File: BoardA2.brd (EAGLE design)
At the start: 44 x 93 mm, 18 parts, among them J1 FEMALE 2x3, T1 2N2222

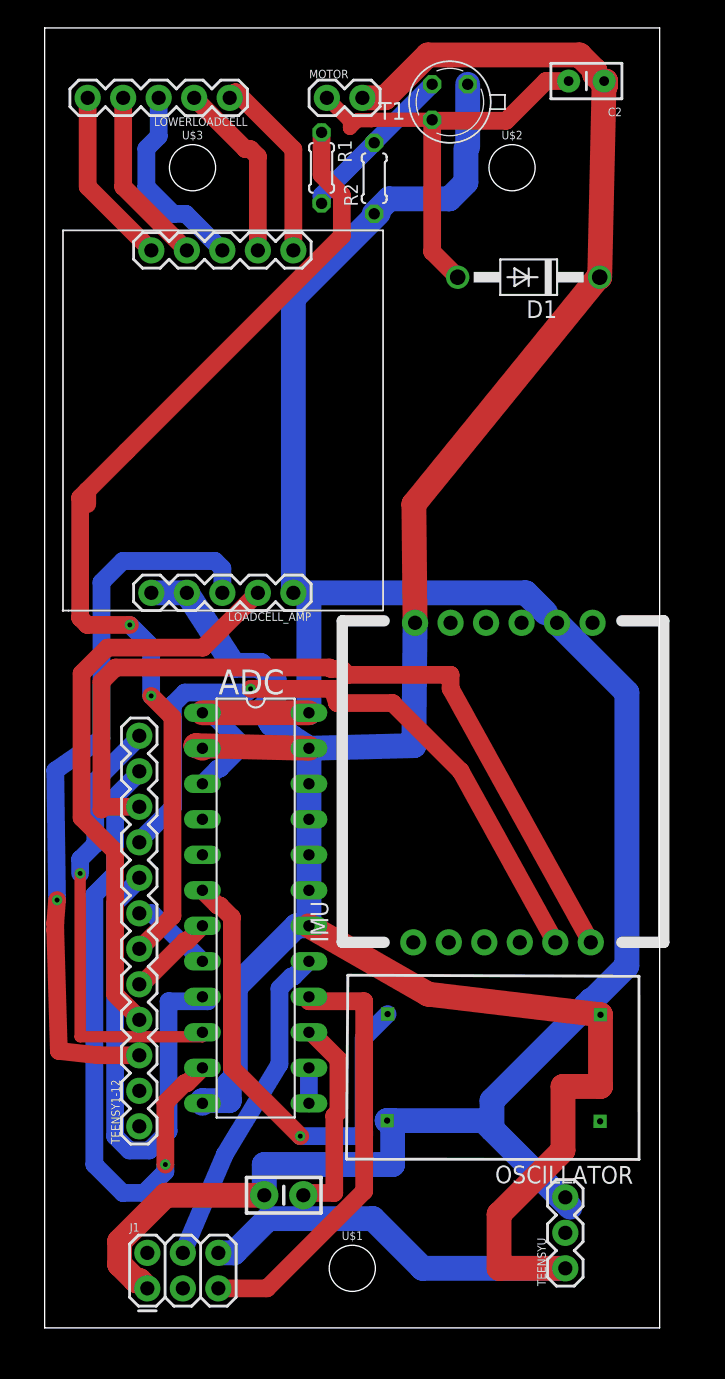
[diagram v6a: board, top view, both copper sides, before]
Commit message: Board2 Missing signal
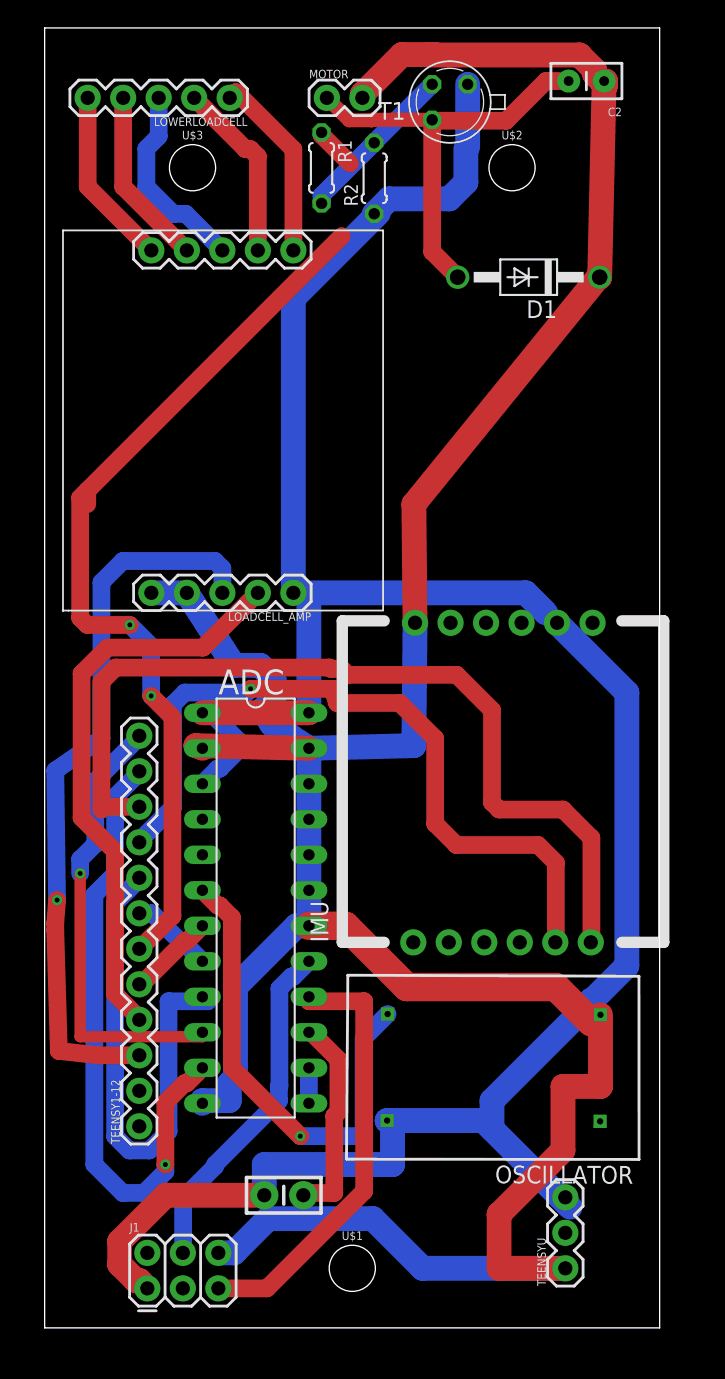
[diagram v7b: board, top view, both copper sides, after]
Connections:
- removed net ADC-CONVST: ADC.5
- new net ADC-CON: ADC.5, TEENSY1-12.2
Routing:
- net MOTOR: track 73.3 -> 68.3 mm
- net IMU-TX: track 48.7 -> 53.5 mm
- net IMU-RX: track 59.3 -> 63.8 mm
- net 5V: track 214.8 -> 216.3 mm
- net ADC-CH2: track 23.5 -> 24.7 mm
- net N$6: track 31.9 -> 31.2 mm
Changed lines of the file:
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@@
 <setting verticaltext="up"/>
 </settings>
-<grid distance="20" unitdist="mil" unit="mm" style="dots" multiple="1" display="yes" altdistance="5" altunitdist="mil" altunit="mm"/>
+<grid distance="20" unitdist="mil" unit="mil" style="dots" multiple="1" display="yes" altdistance="5" altunitdist="mil" altunit="mil"/>
 <layers>
 <layer number="1" name="Top" color="4" fill="1" visible="yes" active="yes"/>
@@
 <wire x1="-2.564" y1="91.5" x2="-2.564" y2="0.96" width="0.1524" layer="231"/>
 <dimension x1="0" y1="0" x2="7.3152" y2="3.429" x3="3.6576" y3="-3.048" textsize="1.778" layer="1" dtype="horizontal"/>
+<dimension x1="6.77" y1="14.42" x2="37.25" y2="4.26" x3="22.01" y3="-7.112" textsize="1.778" layer="1" dtype="horizontal"/>
 </plain>
 <attributes>
@@
 <wire x1="18.907" y1="36.385" x2="18.907" y2="38.925" width="1.778" layer="16"/>
 <wire x1="18.907" y1="38.925" x2="18.907" y2="41.465" width="1.778" layer="16"/>
-<wire x1="18.907" y1="28.765" x2="27.432" y2="23.876" width="1.778" layer="1"/>
-<wire x1="27.432" y1="23.876" x2="39.76725" y2="22.397375" width="1.778" layer="1"/>
 <wire x1="18.907" y1="41.465" x2="10.8204" y2="41.652465625" width="1.778" layer="1"/>
 <wire x1="10.8204" y1="41.652465625" x2="11.287" y2="41.465" width="1.778" layer="1"/>
@@
 <wire x1="18.0242875" y1="28.765" x2="18.907" y2="28.765" width="1.778" layer="16"/>
 <wire x1="13.6492" y1="17.9000875" x2="13.6492" y2="24.3899125" width="1.778" layer="16"/>
-<wire x1="22.731" y1="88" x2="24.3472875" y2="88" width="1.778" layer="1"/>
-<wire x1="24.3472875" y1="88" x2="27.4161875" y2="91.0689" width="1.778" layer="1"/>
+<wire x1="18.907" y1="28.765" x2="21.527" y2="28.765" width="2.032" layer="1"/>
+<wire x1="21.527" y1="28.765" x2="25.908" y2="24.384" width="2.032" layer="1"/>
+<wire x1="36.576" y1="24.384" x2="39.116" y2="21.844" width="2.032" layer="1"/>
+<wire x1="25.908" y1="24.384" x2="36.576" y2="24.384" width="2.032" layer="1"/>
+<wire x1="22.731" y1="88" x2="22.731" y2="88.263" width="1.778" layer="1"/>
+<wire x1="22.731" y1="88.263" x2="25.563" y2="91.095" width="1.778" layer="1"/>
+<wire x1="25.563" y1="91.095" x2="27.94" y2="91.095" width="1.778" layer="1"/>
+<wire x1="27.4161875" y1="91.0689" x2="27.94" y2="91.095" width="0" layer="19" extent="1-1"/>
+<wire x1="39.76725" y1="22.397375" x2="39.116" y2="21.844" width="0" layer="19" extent="1-1"/>
 </signal>
 <signal name="N$1">
@@
 <wire x1="27.724" y1="86.43" x2="23.424025" y2="86.43" width="1.016" layer="1"/>
 <wire x1="23.424025" y1="86.43" x2="23.393825" y2="86.3998" width="1.016" layer="1"/>
-<wire x1="23.393825" y1="86.3998" x2="22.3918" y2="86.3998" width="1.016" layer="1"/>
-<wire x1="22.3918" y1="86.3998" x2="21.844" y2="85.852" width="1.016" layer="1"/>
-<wire x1="21.844" y1="85.852" x2="21.844" y2="86.347" width="1.016" layer="1"/>
-<wire x1="21.844" y1="86.347" x2="20.191" y2="88" width="1.016" layer="1"/>
+<wire x1="23.424025" y1="86.43" x2="23.393825" y2="86.3998" width="1.016" layer="1"/>
+<wire x1="23.393825" y1="86.3998" x2="21.7912" y2="86.3998" width="1.016" layer="1"/>
+<wire x1="21.7912" y1="86.3998" x2="20.191" y2="88" width="1.016" layer="1"/>
 </signal>
 <signal name="N$8">
@@
 <wire x1="6.096" y1="50.292" x2="3.048" y2="50.292" width="1.27" layer="1"/>
 <wire x1="3.048" y1="50.292" x2="2.54" y2="50.8" width="1.27" layer="1"/>
-<wire x1="3.048" y1="58.928" x2="3.048" y2="59.89836875" width="1.27" layer="1"/>
-<wire x1="21.2598" y1="81.0467" x2="19.812" y2="82.4945" width="1.27" layer="1"/>
-<wire x1="19.812" y1="82.4945" x2="19.812" y2="85.527" width="1.27" layer="1"/>
-<wire x1="3.048" y1="59.89836875" x2="5.864815625" y2="62.715184375" width="1.27" layer="1"/>
-<wire x1="5.864815625" y1="62.715184375" x2="21.2598" y2="78.11016875" width="1.27" layer="1"/>
-<wire x1="21.2598" y1="78.11016875" x2="21.2598" y2="81.0467" width="1.27" layer="1"/>
+<wire x1="3.048" y1="59.89836875" x2="3.048" y2="58.928" width="1.27" layer="1"/>
+<wire x1="21.2598" y1="81.0467" x2="19.812" y2="82.4945" width="0" layer="19" extent="1-16"/>
+<wire x1="21.844" y1="83.312" x2="21.2598" y2="78.11016875" width="0" layer="19" extent="1-16"/>
+<wire x1="21.2598" y1="78.11016875" x2="3.048" y2="59.89836875" width="1.27" layer="1"/>
+<wire x1="21.2598" y1="78.11016875" x2="21.2598" y2="81.0467" width="0" layer="19" extent="1-16"/>
 <wire x1="2.54" y1="59.39036875" x2="3.048" y2="59.89836875" width="1.27" layer="1"/>
 <wire x1="2.54" y1="50.8" x2="2.54" y2="59.39036875" width="1.27" layer="1"/>
 <wire x1="7.62" y1="48.768" x2="6.096" y2="50.292" width="1.27" layer="16"/>
 <wire x1="7.62" y1="45.212" x2="7.62" y2="48.768" width="1.27" layer="16"/>
+<wire x1="19.812" y1="85.527" x2="19.812" y2="85.344" width="1.27" layer="1"/>
+<wire x1="19.812" y1="85.344" x2="21.844" y2="83.312" width="1.27" layer="1"/>
 </signal>
 <signal name="AMP-DAT">
@@
 <wire x1="4.064" y1="37.084" x2="4.064" y2="46.228" width="1.27" layer="1"/>
 <wire x1="4.064" y1="46.228" x2="5.08" y2="47.244" width="1.27" layer="1"/>
-<wire x1="29.0416" y1="46.71788125" x2="29.0416" y2="45.7424" width="1.27" layer="1"/>
-<wire x1="29.0416" y1="45.7424" x2="39.073" y2="27.583" width="1.27" layer="1"/>
 <wire x1="5.08" y1="47.244" x2="20.38748125" y2="47.244" width="1.27" layer="1"/>
 <wire x1="21.26428125" y1="47.1424" x2="21.6888" y2="46.71788125" width="1.27" layer="1"/>
-<wire x1="21.6888" y1="46.71788125" x2="29.0416" y2="46.71788125" width="1.27" layer="1"/>
 <wire x1="20.38748125" y1="47.244" x2="20.48908125" y2="47.1424" width="1.27" layer="1"/>
 <wire x1="20.48908125" y1="47.1424" x2="21.26428125" y2="47.1424" width="1.27" layer="1"/>
+<wire x1="29.48211875" y1="46.71788125" x2="32.004" y2="44.196" width="1.27" layer="1"/>
+<wire x1="32.004" y1="44.196" x2="32.004" y2="37.592" width="1.27" layer="1"/>
+<wire x1="32.004" y1="37.592" x2="32.512" y2="37.084" width="1.27" layer="1"/>
+<wire x1="32.512" y1="37.084" x2="37.084" y2="37.084" width="1.27" layer="1"/>
+<wire x1="37.084" y1="37.084" x2="39.116" y2="35.052" width="1.27" layer="1"/>
+<wire x1="39.116" y1="35.052" x2="39.116" y2="27.626" width="1.27" layer="1"/>
+<wire x1="39.116" y1="27.626" x2="39.073" y2="27.583" width="1.27" layer="1"/>
+<wire x1="21.6888" y1="46.71788125" x2="29.48211875" y2="46.71788125" width="1.27" layer="1"/>
 </signal>
 <signal name="IMU-TX">
@@
 <wire x1="9.1788" y1="37.24616875" x2="9.1788" y2="44.6047" width="1.27" layer="16"/>
 <via x="14.732" y="45.72" extent="1-16" drill="0.35"/>
-<wire x1="36.533" y1="27.583" x2="29.769703125" y2="39.826296875" width="1.27" layer="1"/>
-<wire x1="29.769703125" y1="39.826296875" x2="24.892" y2="44.704" width="1.27" layer="1"/>
-<wire x1="20.9159" y1="44.704" x2="24.892" y2="44.704" width="1.27" layer="1"/>
-<wire x1="20.9159" y1="44.704" x2="20.6751" y2="45.4528" width="1.27" layer="1"/>
+<wire x1="20.6751" y1="45.4528" x2="20.9159" y2="44.704" width="1.27" layer="1"/>
 <wire x1="20.6751" y1="45.4528" x2="20.6751" y2="45.72" width="1.27" layer="1"/>
 <wire x1="20.6751" y1="45.72" x2="14.732" y2="45.72" width="1.27" layer="1"/>
+<wire x1="27.94" y1="36.068" x2="29.464" y2="34.544" width="1.27" layer="1"/>
+<wire x1="29.464" y1="34.544" x2="35.306" y2="34.544" width="1.27" layer="1"/>
+<wire x1="35.306" y1="34.544" x2="36.576" y2="33.274" width="1.27" layer="1"/>
+<wire x1="36.576" y1="33.274" x2="36.576" y2="27.626" width="1.27" layer="1"/>
+<wire x1="36.576" y1="27.626" x2="36.533" y2="27.583" width="1.27" layer="1"/>
+<wire x1="20.9159" y1="44.704" x2="25.4" y2="44.704" width="1.27" layer="1"/>
+<wire x1="25.4" y1="44.704" x2="27.94" y2="42.164" width="1.27" layer="1"/>
+<wire x1="27.94" y1="42.164" x2="27.94" y2="36.068" width="1.27" layer="1"/>
 </signal>
 <signal name="ADC-CH1">
@@
 <contactref element="ADC" pad="17"/>
 <contactref element="J1" pad="4"/>
-<wire x1="16.7988" y1="24.2847" x2="17.6469" y2="25.1328" width="1.27" layer="16"/>
+<wire x1="17.6469" y1="25.1328" x2="16.7988" y2="24.2847" width="1.27" layer="16"/>
 <wire x1="17.6469" y1="25.1328" x2="17.8148" y2="25.1328" width="1.27" layer="16"/>
 <wire x1="17.8148" y1="25.1328" x2="18.907" y2="26.225" width="1.27" layer="16"/>
-<wire x1="9.8872" y1="5.366" x2="12.9032" y2="12.4333" width="1.27" layer="16"/>
-<wire x1="12.9032" y1="12.4333" x2="16.7988" y2="18.8689" width="1.27" layer="16"/>
-<wire x1="16.7988" y1="18.8689" x2="16.7988" y2="24.2847" width="1.27" layer="16"/>
+<wire x1="16.7988" y1="17.3068" x2="16.764" y2="17.272" width="1.27" layer="16"/>
+<wire x1="16.764" y1="17.272" x2="16.764" y2="16.256" width="1.27" layer="16"/>
+<wire x1="12.192" y1="11.684" x2="12.192" y2="11.557" width="1.27" layer="16"/>
+<wire x1="12.192" y1="11.557" x2="9.906" y2="9.271" width="1.27" layer="16"/>
+<wire x1="9.906" y1="9.271" x2="9.906" y2="5.3848" width="1.27" layer="16"/>
+<wire x1="9.906" y1="5.3848" x2="9.8872" y2="5.366" width="1.27" layer="16"/>
+<wire x1="16.7988" y1="24.2847" x2="16.7988" y2="17.3068" width="1.27" layer="16"/>
+<wire x1="16.764" y1="16.256" x2="12.192" y2="11.684" width="1.27" layer="16"/>
 </signal>
 <signal name="E+">
@@
 <contactref element="J1" pad="2"/>
 </signal>
-<signal name="ADC-CONVST">
+<signal name="ADC-CON">
 <contactref element="ADC" pad="5"/>
+<contactref element="TEENSY1-12" pad="2"/>
+<wire x1="6.77" y1="16.96" x2="11.287" y2="33.845" width="0" layer="19" extent="1-1"/>
 </signal>
 </signals>
